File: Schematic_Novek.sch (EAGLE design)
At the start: 0 parts

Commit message: Adds stm32f1 uC
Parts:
- added IC1: STM32F10XCXT6, stm32:STM32F10XCXT6
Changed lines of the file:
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@@
 <setting verticaltext="up"/>
 </settings>
-<grid distance="1" unitdist="mm" unit="mm" style="lines" multiple="1" display="yes" altdistance="1" altunitdist="mm" altunit="mm"/>
+<grid distance="0.1" unitdist="inch" unit="inch" style="lines" multiple="1" display="no" altdistance="0.01" altunitdist="inch" altunit="inch"/>
 <layers>
+<layer number="1" name="Top" color="4" fill="1" visible="no" active="no"/>
+<layer number="2" name="Route2" color="1" fill="3" visible="no" active="no"/>
+<layer number="3" name="Route3" color="4" fill="3" visible="no" active="no"/>
+<layer number="4" name="Route4" color="1" fill="4" visible="no" active="no"/>
+<layer number="5" name="Route5" color="4" fill="4" visible="no" active="no"/>
+<layer number="6" name="Route6" color="1" fill="8" visible="no" active="no"/>
+<layer number="7" name="Route7" color="4" fill="8" visible="no" active="no"/>
+<layer number="8" name="Route8" color="1" fill="2" visible="no" active="no"/>
+<layer number="9" name="Route9" color="4" fill="2" visible="no" active="no"/>
+<layer number="10" name="Route10" color="1" fill="7" visible="no" active="no"/>
+<layer number="11" name="Route11" color="4" fill="7" visible="no" active="no"/>
+<layer number="12" name="Route12" color="1" fill="5" visible="no" active="no"/>
+<layer number="13" name="Route13" color="4" fill="5" visible="no" active="no"/>
+<layer number="14" name="Route14" color="1" fill="6" visible="no" active="no"/>
+<layer number="15" name="Route15" color="4" fill="6" visible="no" active="no"/>
+<layer number="16" name="Bottom" color="1" fill="1" visible="no" active="no"/>
+<layer number="17" name="Pads" color="2" fill="1" visible="no" active="no"/>
+<layer number="18" name="Vias" color="2" fill="1" visible="no" active="no"/>
+<layer number="19" name="Unrouted" color="6" fill="1" visible="no" active="no"/>
+<layer number="20" name="Dimension" color="15" fill="1" visible="no" active="no"/>
+<layer number="21" name="tPlace" color="7" fill="1" visible="no" active="no"/>
+<layer number="22" name="bPlace" color="7" fill="1" visible="no" active="no"/>
+<layer number="23" name="tOrigins" color="15" fill="1" visible="no" active="no"/>
+<layer number="24" name="bOrigins" color="15" fill="1" visible="no" active="no"/>
+<layer number="25" name="tNames" color="7" fill="1" visible="no" active="no"/>
+<layer number="26" name="bNames" color="7" fill="1" visible="no" active="no"/>
+<layer number="27" name="tValues" color="7" fill="1" visible="no" active="no"/>
+<layer number="28" name="bValues" color="7" fill="1" visible="no" active="no"/>
+<layer number="29" name="tStop" color="7" fill="3" visible="no" active="no"/>
+<layer number="30" name="bStop" color="7" fill="6" visible="no" active="no"/>
+<layer number="31" name="tCream" color="7" fill="4" visible="no" active="no"/>
+<layer number="32" name="bCream" color="7" fill="5" visible="no" active="no"/>
+<layer number="33" name="tFinish" color="6" fill="3" visible="no" active="no"/>
+<layer number="34" name="bFinish" color="6" fill="6" visible="no" active="no"/>
+<layer number="35" name="tGlue" color="7" fill="4" visible="no" active="no"/>
+<layer number="36" name="bGlue" color="7" fill="5" visible="no" active="no"/>
+<layer number="37" name="tTest" color="7" fill="1" visible="no" active="no"/>
+<layer number="38" name="bTest" color="7" fill="1" visible="no" active="no"/>
+<layer number="39" name="tKeepout" color="4" fill="11" visible="no" active="no"/>
+<layer number="40" name="bKeepout" color="1" fill="11" visible="no" active="no"/>
+<layer number="41" name="tRestrict" color="4" fill="10" visible="no" active="no"/>
+<layer number="42" name="bRestrict" color="1" fill="10" visible="no" active="no"/>
+<layer number="43" name="vRestrict" color="2" fill="10" visible="no" active="no"/>
+<layer number="44" name="Drills" color="7" fill="1" visible="no" active="no"/>
+<layer number="45" name="Holes" color="7" fill="1" visible="no" active="no"/>
+<layer number="46" name="Milling" color="3" fill="1" visible="no" active="no"/>
+<layer number="47" name="Measures" color="7" fill="1" visible="no" active="no"/>
+<layer number="48" name="Document" color="7" fill="1" visible="no" active="no"/>
+<layer number="49" name="Reference" color="7" fill="1" visible="no" active="no"/>
+<layer number="50" name="dxf" color="7" fill="1" visible="no" active="no"/>
+<layer number="51" name="tDocu" color="6" fill="1" visible="no" active="no"/>
+<layer number="52" name="bDocu" color="7" fill="1" visible="no" active="no"/>
 <layer number="88" name="SimResults" color="9" fill="1" visible="yes" active="yes"/>
 <layer number="89" name="SimProbes" color="9" fill="1" visible="yes" active="yes"/>
@@
 <layer number="97" name="Info" color="7" fill="1" visible="yes" active="yes"/>
 <layer number="98" name="Guide" color="6" fill="1" visible="yes" active="yes"/>
+<layer number="100" name="Muster" color="7" fill="1" visible="no" active="no"/>
+<layer number="101" name="Patch_Top" color="12" fill="4" visible="yes" active="yes"/>
+<layer number="116" name="Patch_BOT" color="9" fill="4" visible="yes" active="yes"/>
+<layer number="200" name="200bmp" color="1" fill="10" visible="no" active="no"/>
+<layer number="250" name="Descript" color="3" fill="1" visible="no" active="no"/>
+<layer number="251" name="SMDround" color="12" fill="11" visible="no" active="no"/>
+<layer number="254" name="cooling" color="7" fill="1" visible="yes" active="yes"/>
 </layers>
 <schematic xreflabel="%F%N/%S.%C%R" xrefpart="/%S.%C%R">
@@
 <parts>
 <part name="FRAME1" library="frames" library_urn="urn:adsk.eagle:library:229" deviceset="A4L-LOC" device=""/>
+<part name="IC1" library="stm32" deviceset="STM32F10XCXT6" device=""/>
 </parts>
 <sheets>
@@
 <attribute name="SHEET" x="230.505" y="5.08" size="2.54" layer="94"/>
 </instance>
+<instance part="IC1" gate="PORTA_L" x="109.22" y="124.46" smashed="yes">
+<attribute name="NAME" x="106.68" y="134.62" size="1.27" layer="95"/>
+</instance>
+<instance part="IC1" gate="PORTA_H" x="109.22" y="96.52" smashed="yes">
+<attribute name="NAME" x="106.68" y="109.22" size="1.27" layer="95"/>
+</instance>
+<instance part="IC1" gate="PORTB_L" x="127" y="121.92" smashed="yes">
+<attribute name="NAME" x="121.92" y="134.62" size="1.27" layer="95"/>
+</instance>
+<instance part="IC1" gate="PORTB_H" x="127" y="99.06" smashed="yes">
+<attribute name="NAME" x="121.92" y="109.22" size="1.27" layer="95"/>
+</instance>
+<instance part="IC1" gate="POWER" x="111.76" y="66.04" smashed="yes">
+<attribute name="NAME" x="106.68" y="83.82" size="1.27" layer="95"/>
+</instance>
+<instance part="IC1" gate="PORTC" x="109.22" y="40.64" smashed="yes">
+<attribute name="NAME" x="106.68" y="45.72" size="1.27" layer="95"/>
+</instance>
+<instance part="IC1" gate="PORTD/OSC" x="129.54" y="81.28" smashed="yes">
+<attribute name="NAME" x="121.92" y="83.82" size="1.27" layer="95"/>
+</instance>
+<instance part="IC1" gate="AN_POWER" x="127" y="66.04" smashed="yes">
+<attribute name="NAME" x="121.92" y="73.66" size="1.27" layer="95"/>
+</instance>
+<instance part="IC1" gate="RESET" x="127" y="50.8" smashed="yes">
+<attribute name="VALUE" x="121.92" y="43.18" size="1.27" layer="95"/>
+<attribute name="NAME" x="121.92" y="55.88" size="1.27" layer="95"/>
+</instance>
 </instances>

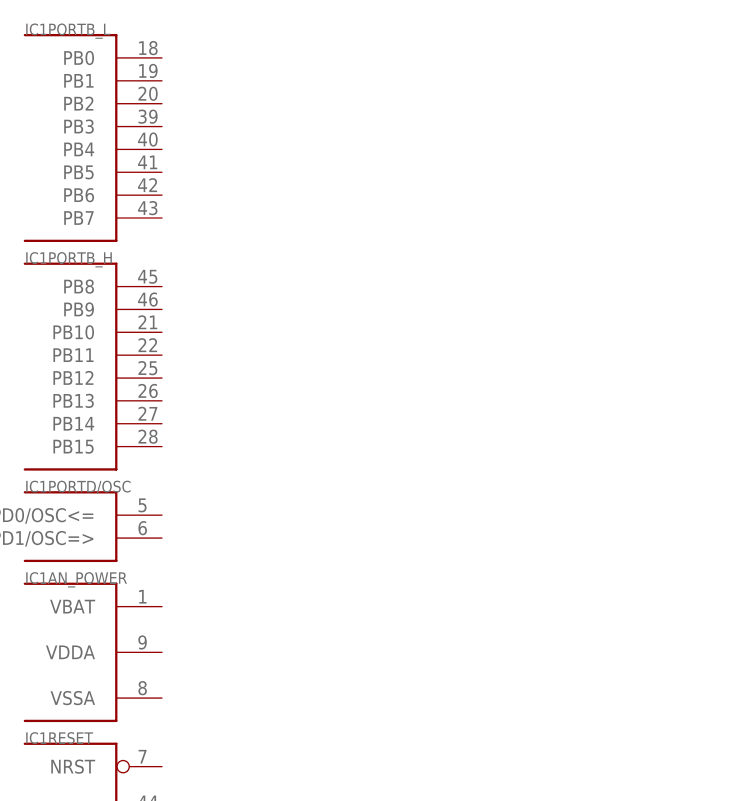
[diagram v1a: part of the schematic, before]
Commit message: Adds HSE 8Mhz clock
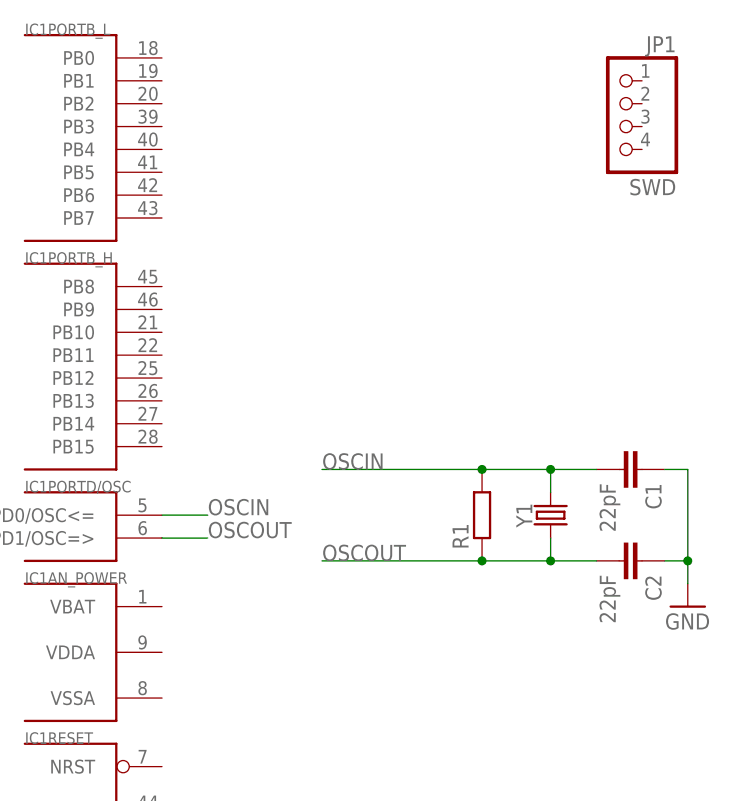
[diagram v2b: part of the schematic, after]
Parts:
- added C1, C2: 22pF, SparkFun-Capacitors:22PF-0603-50V-5%
- added JP1: SWD, pinhead:PINHD-1X4/90
- added R1: (no value), resistor:R-EU_0204/7
- added Y1: (no value), SparkFun-Clocks:CRYSTALPTH-HC49UV
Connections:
- new net GND: C1.1, C2.1
- new net OSCIN: C1.2, IC1PORTD/OSC.PD0/OSC<=, R1.2, Y1.2
- new net OSCOUT: C2.2, IC1PORTD/OSC.PD1/OSC=>, R1.1, Y1.1

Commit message: Adds power sheet
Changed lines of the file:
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@@
 <part name="JP1" library="pinhead" library_urn="urn:adsk.eagle:library:325" deviceset="PINHD-1X4" device="/90" package3d_urn="urn:adsk.eagle:package:22404/2" value="SWD"/>
 <part name="GND1" library="supply1" library_urn="urn:adsk.eagle:library:371" deviceset="GND" device=""/>
+<part name="FRAME2" library="frames" deviceset="A4L-LOC" device=""/>
 </parts>
 <sheets>
@@
 </nets>
 </sheet>
+<sheet>
+<plain>
+</plain>
+<instances>
+<instance part="FRAME2" gate="G$1" x="0" y="0" smashed="yes">
+<attribute name="DRAWING_NAME" x="217.17" y="15.24" size="2.54" layer="94"/>
+<attribute name="LAST_DATE_TIME" x="217.17" y="10.16" size="2.286" layer="94"/>
+<attribute name="SHEET" x="230.505" y="5.08" size="2.54" layer="94"/>
+</instance>
+</instances>
+<busses>
+</busses>
+<nets>
+</nets>
+</sheet>

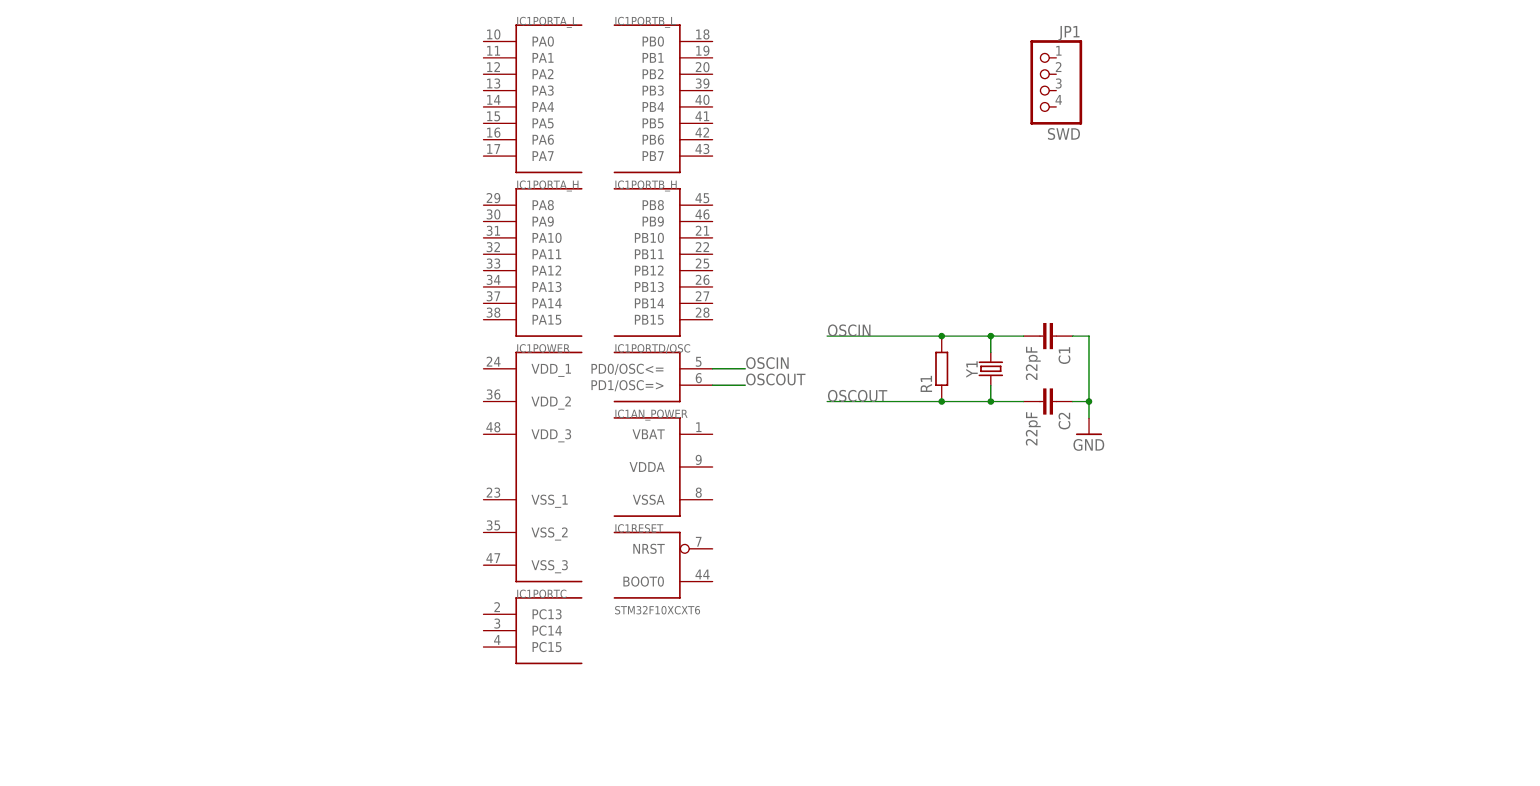
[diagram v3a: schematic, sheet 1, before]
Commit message: Adds reset and power connections to uC
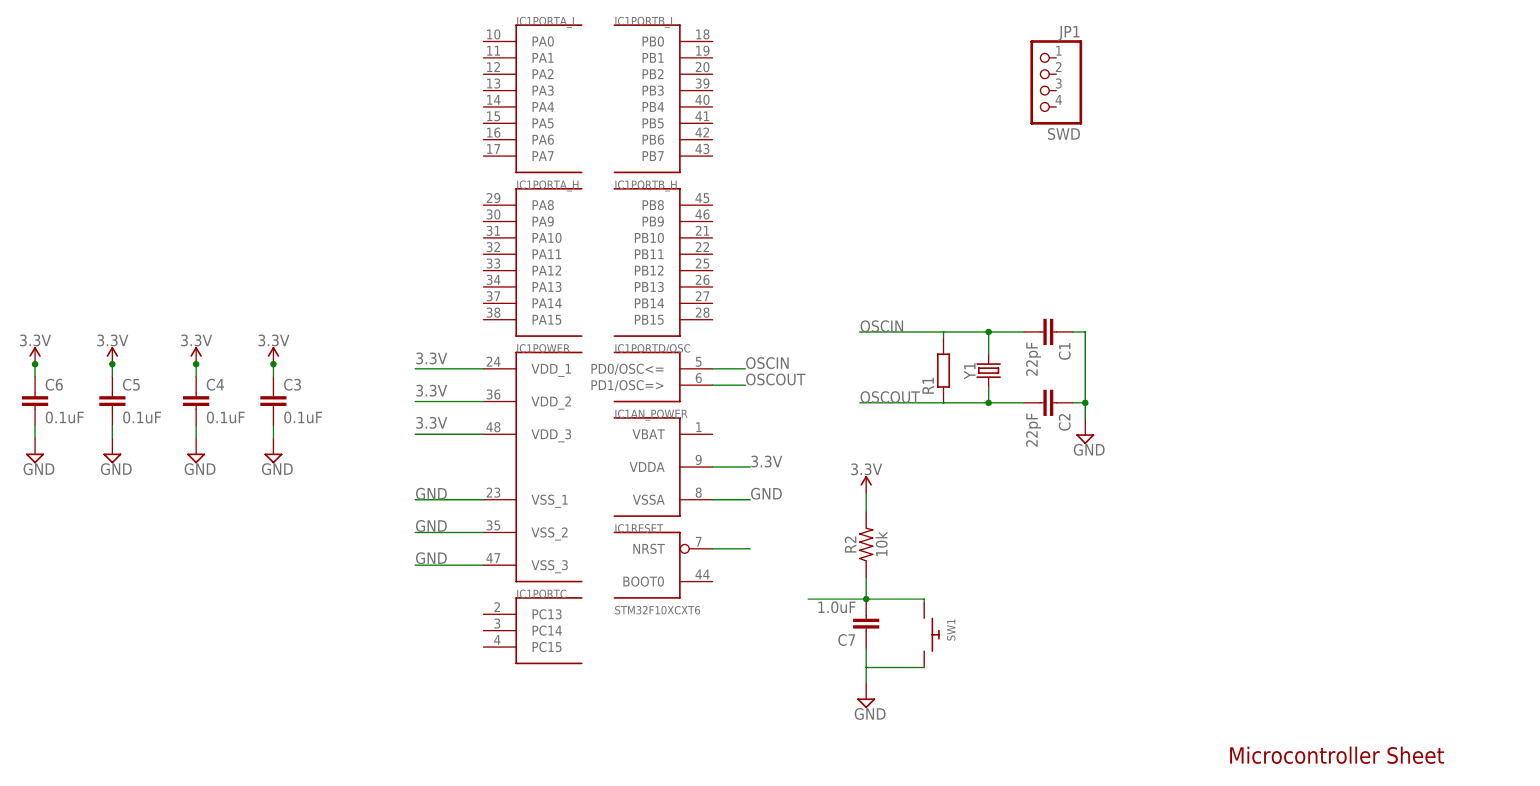
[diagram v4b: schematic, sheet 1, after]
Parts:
- added C3, C4, C5, C6: 0.1uF, SparkFun-Capacitors:0.1UF-0603-25V-(+80/-20%)
- added C7: 1.0uF, SparkFun-Capacitors:1.0UF-0603-16V-10%
- added R2: 10k, SparkFun-Resistors:10KOHM-0603-1/10W-1%
- added SW1: (no value), adafruit:SWITCH_PUSHBUTTONC&K_KSS
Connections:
- new net 3.3V: C3.1, C4.1, C5.1, C6.1, IC1AN_POWER.VDDA, IC1POWER.VDD_1, IC1POWER.VDD_2, IC1POWER.VDD_3, R2.2
- new net N$1: C7.2, R2.1, SW1.P$1
- new net N$2: IC1RESET.NRST
- net GND: now also C3.2, C4.2, C5.2, C6.2, C7.1, IC1AN_POWER.VSSA, IC1POWER.VSS_1, IC1POWER.VSS_2, IC1POWER.VSS_3, SW1.P$2
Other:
- note added: "Microcontroller Sheet"
- note added: "Power Sheet"
- moved on the sheet: C1
